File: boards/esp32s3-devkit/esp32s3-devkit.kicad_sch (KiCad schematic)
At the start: 37 parts, among them J1 Conn_01x17_Pin, J2 Conn_01x17_Pin, J3 USB_C_Receptacle_USB2.0_14P, Q1 Q_PMOS_GSD, SW1 ON/OFF, SW2 RESET, SW3 BOOT, U1 TPS630701RNMR, U2 ESP32-S3-WROOM-1, U3 USBLC6-2SC6

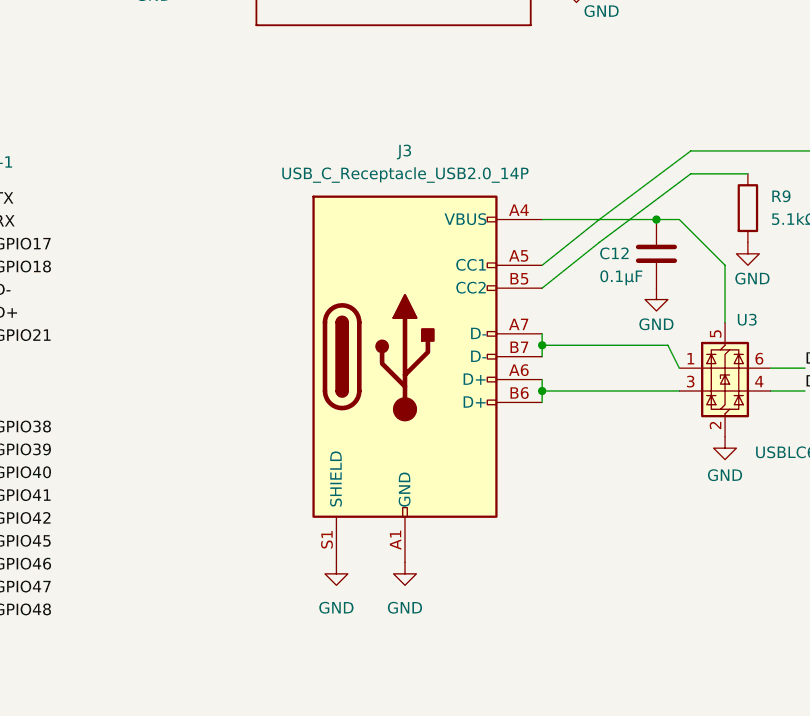
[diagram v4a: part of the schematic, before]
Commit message: fix(esp32s3-devkit): migrate J3 USB-C to 16P symbol and Connector_USB footprint.
Use KiCad Connector USB‑C USB2 16P (A8/B8 SH) with the KiCad Connector_USB HRO footprint, remove the duplicated HRO footprint lib, refresh PCB pad SH naming, and add a small migration helper script.
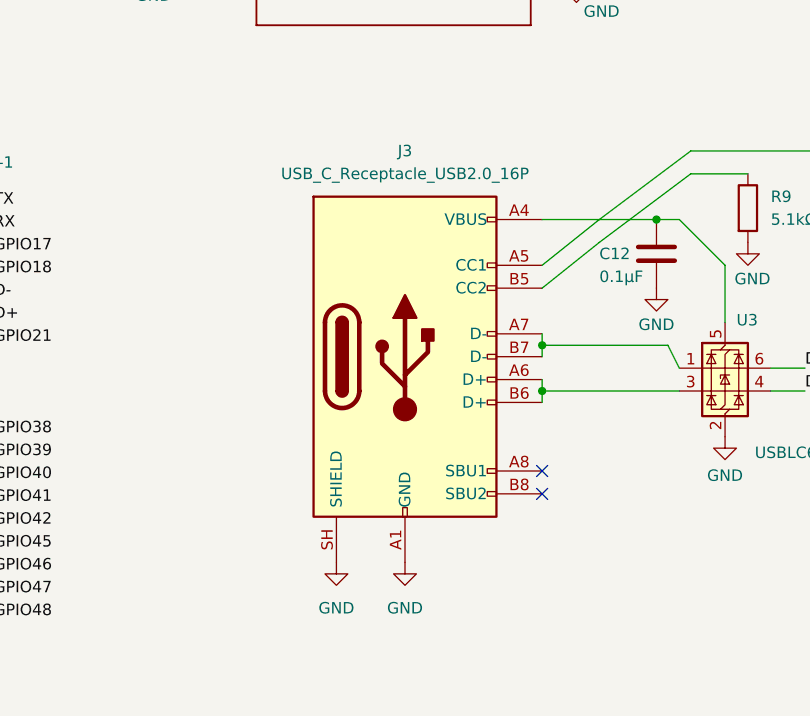
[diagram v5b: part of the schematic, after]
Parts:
- J3: value USB_C_Receptacle_USB2.0_14P -> USB_C_Receptacle_USB2.0_16P; footprint HRO_TypeC_USB:USB_C_Receptacle_HRO_TYPE-C-31-M-12 -> Connector_USB:USB_C_Receptacle_HRO_TYPE-C-31-M-12; symbol Connector:USB_C_Receptacle_USB2.0_14P -> Connector:USB_C_Receptacle_USB2.0_16P
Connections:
- net GND: now also J3.SH (SHIELD); no longer J3.S1 (SHIELD)
- no-connect marks 3 -> 5
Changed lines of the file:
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@@
 	)
 	(no_connect
+		(at 167.64 143.51)
+	)
+	(no_connect
 		(at 106.68 132.08)
 	)
@@
 		(at 106.68 134.62)
 	)
+	(no_connect
+		(at 167.64 146.05)
+	)
 	(wire
 		(pts
@@
 	(wire
 		(pts
+			(xy 101.6 46.99) (xy 105.41 46.99)
+		)
+		(stroke
+			(width 0)
+			(type default)
+		)
+	)
+	(wire
+		(pts
 			(xy 167.64 129.54) (xy 167.64 130.81)
 		)
@@
 	(wire
 		(pts
-			(xy 101.6 46.99) (xy 105.41 46.99)
-		)
-		(stroke
-			(width 0)
-			(type default)
-		)
-	)
-	(wire
-		(pts
 			(xy 173.99 54.61) (xy 179.07 54.61)
 		)
@@
 	(symbol
 		(lib_id "power:PWR_FLAG")
-		(at 101.6 46.99 0)
-		(unit 1)
-		(body_style 1)
-		(exclude_from_sim no)
-		(in_bom yes)
-		(on_board yes)
-		(in_pos_files yes)
-		(dnp no)
-		(property "Reference" "#FLG04"
-			(at 101.6 45.085 0)
-			(hide yes)
-			(show_name no)
-			(do_not_autoplace no)
-			(effects
-				(font
-					(size 1.27 1.27)
-				)
-			)
-		)
-		(property "Value" "PWR_FLAG"
-			(at 104.648 41.91 0)
-			(show_name no)
-			(do_not_autoplace no)
-			(effects
-				(font
-					(size 1.27 1.27)
-				)
-			)
-		)
-		(property "Footprint" ""
-			(at 101.6 46.99 0)
-			(hide yes)
-			(show_name no)
-			(do_not_autoplace no)
-			(effects
-				(font
-					(size 1.27 1.27)
-				)
-			)
-		)
-		(property "Datasheet" ""
-			(at 101.6 46.99 0)
-			(hide yes)
-			(show_name no)
-			(do_not_autoplace no)
-			(effects
-				(font
-					(size 1.27 1.27)
-				)
-			)
-		)
-		(property "Description" "Special symbol for telling ERC where power comes from"
-			(at 101.6 46.99 0)
-			(hide yes)
-			(show_name no)
-			(do_not_autoplace no)
-			(effects
-				(font
-					(size 1.27 1.27)
-				)
-			)
-		)
-		(pin "1"
-		)
-		(instances
-			(project "esp32s3-devkit"
-				(path "/7924bd8b-2498-4d76-899d-c0ad5a514485"
-					(reference "#FLG04")
-					(unit 1)
-				)
-			)
-		)
-	)
-	(symbol
-		(lib_id "power:PWR_FLAG")
 		(at 236.22 106.68 0)
 		(unit 1)
@@
 	)
 	(symbol
-		(lib_id "Connector:USB_C_Receptacle_USB2.0_14P")
+		(lib_id "Connector:USB_C_Receptacle_USB2.0_16P")
 		(at 152.4 130.81 0)
 		(unit 1)
@@
 			)
 		)
-		(property "Value" "USB_C_Receptacle_USB2.0_14P"
+		(property "Value" "USB_C_Receptacle_USB2.0_16P"
 			(at 152.4 110.49 0)
 			(show_name no)
@@
 			)
 		)
-		(property "Footprint" "HRO_TypeC_USB:USB_C_Receptacle_HRO_TYPE-C-31-M-12"
+		(property "Footprint" "Connector_USB:USB_C_Receptacle_HRO_TYPE-C-31-M-12"
 			(at 156.21 130.81 0)
 			(hide yes)
@@
 			)
 		)
-		(property "Description" "USB 2.0-only 14P Type-C Receptacle connector"
+		(property "Description" "USB 2.0-only 16P Type-C Receptacle connector"
 			(at 152.4 130.81 0)
 			(hide yes)
@@
 		(pin "A1"
 		)
-		(pin "A12"
-		)
-		(pin "B1"
+		(pin "A4"
 		)
-		(pin "B6"
+		(pin "A5"
 		)
 		(pin "A6"
 		)
-		(pin "B7"
-		)
 		(pin "A7"
 		)
-		(pin "B5"
+		(pin "A8"
 		)
-		(pin "A5"
+		(pin "A9"
 		)
-		(pin "B9"
+		(pin "A12"
+		)
+		(pin "B1"
 		)
 		(pin "B4"
 		)
-		(pin "A9"
+		(pin "B5"
 		)
-		(pin "A4"
+		(pin "B6"
+		)
+		(pin "B7"
+		)
+		(pin "B8"
+		)
+		(pin "B9"
 		)
 		(pin "B12"
 		)
-		(pin "S1"
+		(pin "SH"
 		)
 		(instances
@@
 					(unit 1)
 				)
+			)
+		)
+	)
+	(symbol
+		(lib_id "power:PWR_FLAG")
+		(at 101.6 46.99 0)
+		(unit 1)
+		(body_style 1)
+		(exclude_from_sim no)
+		(in_bom yes)
+		(on_board yes)
+		(in_pos_files yes)
+		(dnp no)
+		(property "Reference" "#FLG04"
+			(at 101.6 45.085 0)
+			(hide yes)
+			(show_name no)
+			(do_not_autoplace no)
+			(effects
+				(font
+					(size 1.27 1.27)
+				)
+			)
+		)
+		(property "Value" "PWR_FLAG"
+			(at 104.648 41.91 0)
+			(show_name no)
+			(do_not_autoplace no)
+			(effects
+				(font
+					(size 1.27 1.27)
+				)
+			)
+		)
+		(property "Footprint" ""
+			(at 101.6 46.99 0)
+			(hide yes)
+			(show_name no)
+			(do_not_autoplace no)
+			(effects
+				(font
+					(size 1.27 1.27)
+				)
+			)
+		)
+		(property "Datasheet" ""
+			(at 101.6 46.99 0)
+			(hide yes)
+			(show_name no)
+			(do_not_autoplace no)
+			(effects
+				(font
+					(size 1.27 1.27)
+				)
+			)
+		)
+		(property "Description" "Special symbol for telling ERC where power comes from"
+			(at 101.6 46.99 0)
+			(hide yes)
+			(show_name no)
+			(do_not_autoplace no)
+			(effects
+				(font
+					(size 1.27 1.27)
+				)
+			)
+		)
+		(pin "1"
+		)
+		(instances
+			(project "esp32s3-devkit"
+				(path "/7924bd8b-2498-4d76-899d-c0ad5a514485"
+					(reference "#FLG04")
+					(unit 1)
+				)

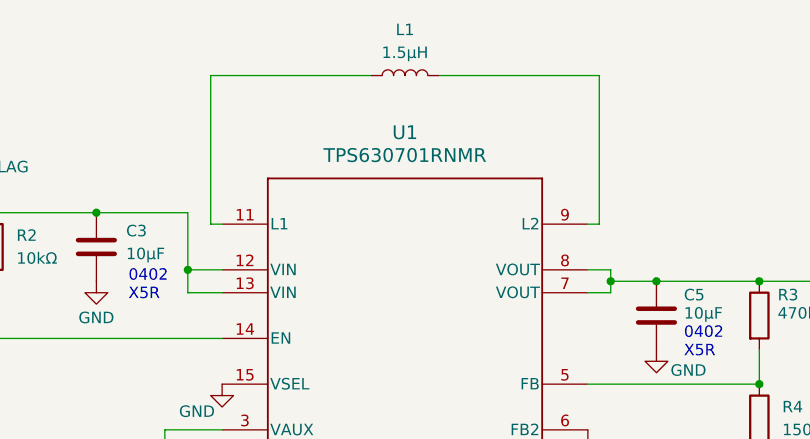
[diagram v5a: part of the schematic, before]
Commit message: fix(esp32s3-devkit): use adjustable TPS63070 instead of fixed TPS630701
The schematic uses a resistor divider (R3=470k, R4=150k) on the FB pin
to regulate output to 3.3V, which requires the adjustable TPS63070RNMR.
The fixed TPS630701RNMR ignores the external divider and outputs 5V.

Renames the library symbol, schematic references, and PCB value to
TPS63070RNMR throughout. Also adds JLCPCB BOM and CPL assembly files.
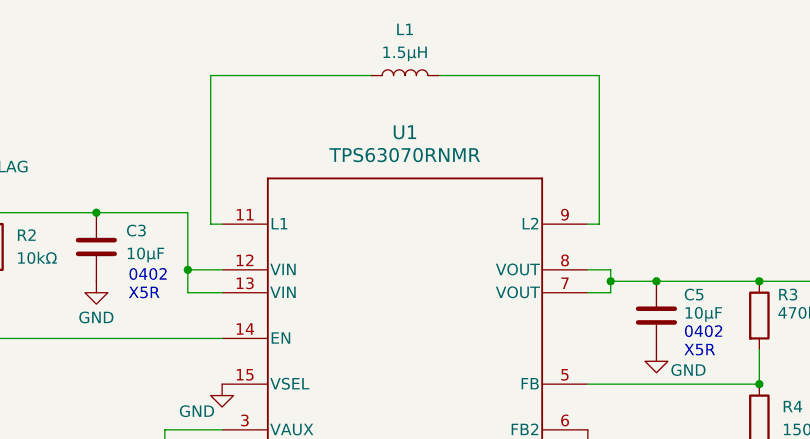
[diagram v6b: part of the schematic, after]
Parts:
- U1: value TPS630701RNMR -> TPS63070RNMR; symbol TPS630701 Buck-Boost:TPS630701RNMR -> TPS63070 Buck-Boost:TPS63070RNMR
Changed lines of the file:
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@@
 	)
 	(symbol
-		(lib_id "TPS630701 Buck-Boost:TPS630701RNMR")
+		(lib_id "TPS63070 Buck-Boost:TPS63070RNMR")
 		(at 151.13 68.58 0)
 		(unit 1)
@@
 			)
 		)
-		(property "Value" "TPS630701RNMR"
+		(property "Value" "TPS63070RNMR"
 			(at 151.13 40.64 0)
 			(show_name no)

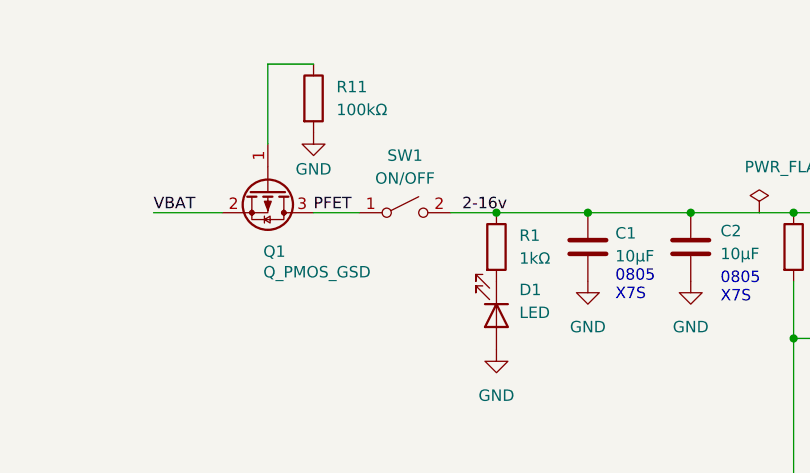
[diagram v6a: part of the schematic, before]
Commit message: fix(esp32s3-devkit): replace SW1 with MK-12C03-G015 slide switch for JLCPCB availability
The original CK RS282G05A3 SPST switch (C2804704) is out of stock at
JLCPCB. Replace with G-Switch MK-12C03-G015 SPDT slide switch
(C2890358, ~4900 in stock) using KiCad's built-in
SW_SPDT_Shouhan_MSK12C02 footprint (same package family).

Schematic changes:
- SW1 symbol changed from SW_SPST to SW_SPDT
- Pin 2 (COM) connects to /PFET, pin 1 (Throw A) to /2-16v
- Pin 3 (Throw B) marked no-connect
- Footprint updated to Button_Switch_SMD:SW_SPDT_Shouhan_MSK12C02

BOM sync with user's JLCPCB part selections:
- D1/D3: C72043 -> C2286 (red LED, in stock)
- D2: C2928910 -> C493210 (BZT52B3V6S 3.6V Zener, in stock)
- SW1: C2804704 -> C2890358 (MK-12C03-G015 slide switch)

NOTE: PCB layout update required - user must run "Update PCB from
Schematic" in KiCad, place/route the new SW1 footprint, run DRC,
and regenerate Gerber files + CPL.
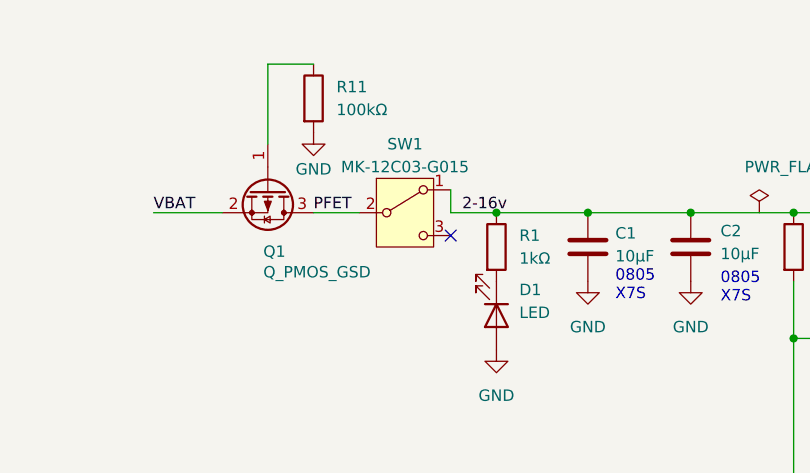
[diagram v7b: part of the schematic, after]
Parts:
- SW1: value ON/OFF -> MK-12C03-G015; footprint Button_Switch_SMD:SW_SPST_CK_RS282G05A3 -> Button_Switch_SMD:SW_SPDT_Shouhan_MSK12C02; symbol Switch:SW_SPST -> Switch:SW_SPDT
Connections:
- net 2-16v: now also SW1.1 (A); no longer SW1.2 (B)
- net PFET: now also SW1.2 (B); no longer SW1.1 (A)
- no-connect marks 5 -> 6
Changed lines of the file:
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@@
 		(at 167.64 146.05)
 	)
+	(no_connect
+		(at 67.31 49.53)
+	)
 	(wire
 		(pts
@@
 		(pts
 			(xy 66.04 121.92) (xy 73.66 121.92)
+		)
+		(stroke
+			(width 0)
+			(type default)
+		)
+	)
+	(wire
+		(pts
+			(xy 67.31 44.45) (xy 67.31 46.99)
 		)
 		(stroke
@@
 	)
 	(symbol
-		(lib_id "Switch:SW_SPST")
+		(lib_id "Switch:SW_SPDT")
 		(at 62.23 46.99 0)
 		(unit 1)
@@
 		(fields_autoplaced yes)
 		(property "Reference" "SW1"
-			(at 62.23 40.64 0)
-			(show_name no)
-			(do_not_autoplace no)
-			(effects
-				(font
-					(size 1.27 1.27)
-				)
-			)
-		)
-		(property "Value" "ON/OFF"
-			(at 62.23 43.18 0)
-			(show_name no)
-			(do_not_autoplace no)
-			(effects
-				(font
-					(size 1.27 1.27)
-				)
-			)
-		)
-		(property "Footprint" "Button_Switch_SMD:SW_SPST_CK_RS282G05A3"
+			(at 62.23 39.37 0)
+			(show_name no)
+			(do_not_autoplace no)
+			(effects
+				(font
+					(size 1.27 1.27)
+				)
+			)
+		)
+		(property "Value" "MK-12C03-G015"
+			(at 62.23 41.91 0)
+			(show_name no)
+			(do_not_autoplace no)
+			(effects
+				(font
+					(size 1.27 1.27)
+				)
+			)
+		)
+		(property "Footprint" "Button_Switch_SMD:SW_SPDT_Shouhan_MSK12C02"
 			(at 62.23 46.99 0)
 			(hide yes)
@@
 			)
 		)
-		(property "Description" "Single Pole Single Throw (SPST) switch"
+		(property "Description" "Switch, single pole double throw"
 			(at 62.23 46.99 0)
 			(hide yes)
@@
 			)
 		)
+		(pin "1"
+		)
 		(pin "2"
 		)
-		(pin "1"
+		(pin "3"
 		)
 		(instances
